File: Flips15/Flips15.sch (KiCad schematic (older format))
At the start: 6 parts

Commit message: Flips15 to only use 1 unit
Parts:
- removed CNX101: UFP2810, Own:Pin_Header_Angle_Shrouded_2x05_Pitch2.54mm_ConvNumbering, symbol Eigene~Bauteile:UFP2810
- added JP101, JP102, JP103, JP104, JP105, JP106, JP107, JP108, JP109, JP110, JP111, JP112, JP113, JP114, JP115, JP116, JP117, JP118, JP119, JP120, JP121, JP122, JP123, JP124, JP125, JP126, JP127, JP128: Jumper_NO_Small, Own:SolderJumper1.3mm, symbol Device:Jumper_NO_Small
- BRDIC1: renamed from BRDIC101; footprint Own:Pin_Header_Angle_Shrouded_2x17_Pitch2.54mm_ConvNumbering -> Own:Pin_Header_Straight_Shrouded_Locks_2x17_Pitch2.54mm_ConvNumbering
- BROSE20: renamed from BROSE103; footprint Own:Pin_Header_Straight_Shrouded_2x10_Pitch2.54mm_ConvNumbering -> Own:Pin_Header_Straight_Shrouded_Locks_2x10_Pitch2.54mm_ConvNumbering
- BROSE34: renamed from BROSE102; footprint Own:Pin_Header_Angle_Shrouded_2x17_Pitch2.54mm_ConvNumbering -> Own:Pin_Header_Straight_Shrouded_Locks_2x17_Pitch2.54mm_ConvNumbering
- BROSE60: renamed from BROSE101; footprint Own:Pin_Header_Straight_Shrouded_2x30_Pitch2.54mm_ConvNumbering -> Own:Pin_Header_Straight_Shrouded_Locks_2x30_Pitch2.54mm_ConvNumbering
- renumbered CNY101 to CN1
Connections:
- wire segments 160 -> 80
- no-connect marks 66 -> 58

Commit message: experimenting with solder jumpers at BRDIC1 connector
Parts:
- JP101, JP102, JP103, JP104, JP105, JP106, JP107, JP108, JP109, JP110, JP111, JP112, JP113, JP114, JP115, JP116, JP117, JP118, JP119, JP120, JP121, JP122, JP123, JP124, JP125, JP126, JP127, JP128: footprint Own:SolderJumper1.3mm -> Own:SolderJumper1.3mmNoSilk
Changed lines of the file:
@@
 F 0 "JP114" H 7900 3393 50  0000 C CNN
 F 1 "Jumper_NO_Small" H 7900 3394 50  0001 C CNN
-F 2 "Own:SolderJumper1.3mm" H 7900 3300 50  0001 C CNN
+F 2 "Own:SolderJumper1.3mmNoSilk" H 7900 3300 50  0001 C CNN
 F 3 "~" H 7900 3300 50  0001 C CNN
 	1    7900 3300
@@
 F 0 "JP113" H 7900 3293 50  0000 C CNN
 F 1 "Jumper_NO_Small" H 7900 3294 50  0001 C CNN
-F 2 "Own:SolderJumper1.3mm" H 7900 3200 50  0001 C CNN
+F 2 "Own:SolderJumper1.3mmNoSilk" H 7900 3200 50  0001 C CNN
 F 3 "~" H 7900 3200 50  0001 C CNN
 	1    7900 3200
@@
 F 0 "JP112" H 7900 3193 50  0000 C CNN
 F 1 "Jumper_NO_Small" H 7900 3194 50  0001 C CNN
-F 2 "Own:SolderJumper1.3mm" H 7900 3100 50  0001 C CNN
+F 2 "Own:SolderJumper1.3mmNoSilk" H 7900 3100 50  0001 C CNN
 F 3 "~" H 7900 3100 50  0001 C CNN
 	1    7900 3100
@@
 F 0 "JP111" H 7900 3093 50  0000 C CNN
 F 1 "Jumper_NO_Small" H 7900 3094 50  0001 C CNN
-F 2 "Own:SolderJumper1.3mm" H 7900 3000 50  0001 C CNN
+F 2 "Own:SolderJumper1.3mmNoSilk" H 7900 3000 50  0001 C CNN
 F 3 "~" H 7900 3000 50  0001 C CNN
 	1    7900 3000
@@
 F 0 "JP110" H 7900 2993 50  0000 C CNN
 F 1 "Jumper_NO_Small" H 7900 2994 50  0001 C CNN
-F 2 "Own:SolderJumper1.3mm" H 7900 2900 50  0001 C CNN
+F 2 "Own:SolderJumper1.3mmNoSilk" H 7900 2900 50  0001 C CNN
 F 3 "~" H 7900 2900 50  0001 C CNN
 	1    7900 2900
@@
 F 0 "JP109" H 7900 2893 50  0000 C CNN
 F 1 "Jumper_NO_Small" H 7900 2894 50  0001 C CNN
-F 2 "Own:SolderJumper1.3mm" H 7900 2800 50  0001 C CNN
+F 2 "Own:SolderJumper1.3mmNoSilk" H 7900 2800 50  0001 C CNN
 F 3 "~" H 7900 2800 50  0001 C CNN
 	1    7900 2800
@@
 F 0 "JP108" H 7900 2793 50  0000 C CNN
 F 1 "Jumper_NO_Small" H 7900 2794 50  0001 C CNN
-F 2 "Own:SolderJumper1.3mm" H 7900 2700 50  0001 C CNN
+F 2 "Own:SolderJumper1.3mmNoSilk" H 7900 2700 50  0001 C CNN
 F 3 "~" H 7900 2700 50  0001 C CNN
 	1    7900 2700
@@
 F 0 "JP107" H 7900 2293 50  0000 C CNN
 F 1 "Jumper_NO_Small" H 7900 2294 50  0001 C CNN
-F 2 "Own:SolderJumper1.3mm" H 7900 2200 50  0001 C CNN
+F 2 "Own:SolderJumper1.3mmNoSilk" H 7900 2200 50  0001 C CNN
 F 3 "~" H 7900 2200 50  0001 C CNN
 	1    7900 2200
@@
 F 0 "JP106" H 7900 2193 50  0000 C CNN
 F 1 "Jumper_NO_Small" H 7900 2194 50  0001 C CNN
-F 2 "Own:SolderJumper1.3mm" H 7900 2100 50  0001 C CNN
+F 2 "Own:SolderJumper1.3mmNoSilk" H 7900 2100 50  0001 C CNN
 F 3 "~" H 7900 2100 50  0001 C CNN
 	1    7900 2100
@@
 F 0 "JP105" H 7900 2093 50  0000 C CNN
 F 1 "Jumper_NO_Small" H 7900 2094 50  0001 C CNN
-F 2 "Own:SolderJumper1.3mm" H 7900 2000 50  0001 C CNN
+F 2 "Own:SolderJumper1.3mmNoSilk" H 7900 2000 50  0001 C CNN
 F 3 "~" H 7900 2000 50  0001 C CNN
 	1    7900 2000
@@
 F 0 "JP104" H 7900 1993 50  0000 C CNN
 F 1 "Jumper_NO_Small" H 7900 1994 50  0001 C CNN
-F 2 "Own:SolderJumper1.3mm" H 7900 1900 50  0001 C CNN
+F 2 "Own:SolderJumper1.3mmNoSilk" H 7900 1900 50  0001 C CNN
 F 3 "~" H 7900 1900 50  0001 C CNN
 	1    7900 1900
@@
 F 0 "JP103" H 7900 1893 50  0000 C CNN
 F 1 "Jumper_NO_Small" H 7900 1894 50  0001 C CNN
-F 2 "Own:SolderJumper1.3mm" H 7900 1800 50  0001 C CNN
+F 2 "Own:SolderJumper1.3mmNoSilk" H 7900 1800 50  0001 C CNN
 F 3 "~" H 7900 1800 50  0001 C CNN
 	1    7900 1800
@@
 F 0 "JP102" H 7900 1793 50  0000 C CNN
 F 1 "Jumper_NO_Small" H 7900 1794 50  0001 C CNN
-F 2 "Own:SolderJumper1.3mm" H 7900 1700 50  0001 C CNN
+F 2 "Own:SolderJumper1.3mmNoSilk" H 7900 1700 50  0001 C CNN
 F 3 "~" H 7900 1700 50  0001 C CNN
 	1    7900 1700
@@
 F 0 "JP101" H 7900 1693 50  0000 C CNN
 F 1 "Jumper_NO_Small" H 7900 1694 50  0001 C CNN
-F 2 "Own:SolderJumper1.3mm" H 7900 1600 50  0001 C CNN
+F 2 "Own:SolderJumper1.3mmNoSilk" H 7900 1600 50  0001 C CNN
 F 3 "~" H 7900 1600 50  0001 C CNN
 	1    7900 1600
@@
 F 0 "JP121" H 7900 4493 50  0000 C CNN
 F 1 "Jumper_NO_Small" H 7900 4494 50  0001 C CNN
-F 2 "Own:SolderJumper1.3mm" H 7900 4400 50  0001 C CNN
+F 2 "Own:SolderJumper1.3mmNoSilk" H 7900 4400 50  0001 C CNN
 F 3 "~" H 7900 4400 50  0001 C CNN
 	1    7900 4400
@@
 F 0 "JP120" H 7900 4393 50  0000 C CNN
 F 1 "Jumper_NO_Small" H 7900 4394 50  0001 C CNN
-F 2 "Own:SolderJumper1.3mm" H 7900 4300 50  0001 C CNN
+F 2 "Own:SolderJumper1.3mmNoSilk" H 7900 4300 50  0001 C CNN
 F 3 "~" H 7900 4300 50  0001 C CNN
 	1    7900 4300
@@
 F 0 "JP119" H 7900 4293 50  0000 C CNN
 F 1 "Jumper_NO_Small" H 7900 4294 50  0001 C CNN
-F 2 "Own:SolderJumper1.3mm" H 7900 4200 50  0001 C CNN
+F 2 "Own:SolderJumper1.3mmNoSilk" H 7900 4200 50  0001 C CNN
 F 3 "~" H 7900 4200 50  0001 C CNN
 	1    7900 4200
@@
 F 0 "JP118" H 7900 4193 50  0000 C CNN
 F 1 "Jumper_NO_Small" H 7900 4194 50  0001 C CNN
-F 2 "Own:SolderJumper1.3mm" H 7900 4100 50  0001 C CNN
+F 2 "Own:SolderJumper1.3mmNoSilk" H 7900 4100 50  0001 C CNN
 F 3 "~" H 7900 4100 50  0001 C CNN
 	1    7900 4100
@@
 F 0 "JP117" H 7900 4093 50  0000 C CNN
 F 1 "Jumper_NO_Small" H 7900 4094 50  0001 C CNN
-F 2 "Own:SolderJumper1.3mm" H 7900 4000 50  0001 C CNN
+F 2 "Own:SolderJumper1.3mmNoSilk" H 7900 4000 50  0001 C CNN
 F 3 "~" H 7900 4000 50  0001 C CNN
 	1    7900 4000
@@
 F 0 "JP116" H 7900 3993 50  0000 C CNN
 F 1 "Jumper_NO_Small" H 7900 3994 50  0001 C CNN
-F 2 "Own:SolderJumper1.3mm" H 7900 3900 50  0001 C CNN
+F 2 "Own:SolderJumper1.3mmNoSilk" H 7900 3900 50  0001 C CNN
 F 3 "~" H 7900 3900 50  0001 C CNN
 	1    7900 3900
@@
 F 0 "JP115" H 7900 3893 50  0000 C CNN
 F 1 "Jumper_NO_Small" H 7900 3894 50  0001 C CNN
-F 2 "Own:SolderJumper1.3mm" H 7900 3800 50  0001 C CNN
+F 2 "Own:SolderJumper1.3mmNoSilk" H 7900 3800 50  0001 C CNN
 F 3 "~" H 7900 3800 50  0001 C CNN
 	1    7900 3800
@@
 F 0 "JP128" H 7900 5593 50  0000 C CNN
 F 1 "Jumper_NO_Small" H 7900 5594 50  0001 C CNN
-F 2 "Own:SolderJumper1.3mm" H 7900 5500 50  0001 C CNN
+F 2 "Own:SolderJumper1.3mmNoSilk" H 7900 5500 50  0001 C CNN
 F 3 "~" H 7900 5500 50  0001 C CNN
 	1    7900 5500
@@
 F 0 "JP127" H 7900 5493 50  0000 C CNN
 F 1 "Jumper_NO_Small" H 7900 5494 50  0001 C CNN
-F 2 "Own:SolderJumper1.3mm" H 7900 5400 50  0001 C CNN
+F 2 "Own:SolderJumper1.3mmNoSilk" H 7900 5400 50  0001 C CNN
 F 3 "~" H 7900 5400 50  0001 C CNN
 	1    7900 5400
@@
 F 0 "JP126" H 7900 5393 50  0000 C CNN
 F 1 "Jumper_NO_Small" H 7900 5394 50  0001 C CNN
-F 2 "Own:SolderJumper1.3mm" H 7900 5300 50  0001 C CNN
+F 2 "Own:SolderJumper1.3mmNoSilk" H 7900 5300 50  0001 C CNN
 F 3 "~" H 7900 5300 50  0001 C CNN
 	1    7900 5300
@@
 F 0 "JP125" H 7900 5293 50  0000 C CNN
 F 1 "Jumper_NO_Small" H 7900 5294 50  0001 C CNN
-F 2 "Own:SolderJumper1.3mm" H 7900 5200 50  0001 C CNN
+F 2 "Own:SolderJumper1.3mmNoSilk" H 7900 5200 50  0001 C CNN
 F 3 "~" H 7900 5200 50  0001 C CNN
 	1    7900 5200
@@
 F 0 "JP124" H 7900 5193 50  0000 C CNN
 F 1 "Jumper_NO_Small" H 7900 5194 50  0001 C CNN
-F 2 "Own:SolderJumper1.3mm" H 7900 5100 50  0001 C CNN
+F 2 "Own:SolderJumper1.3mmNoSilk" H 7900 5100 50  0001 C CNN
 F 3 "~" H 7900 5100 50  0001 C CNN
 	1    7900 5100
@@
 F 0 "JP123" H 7900 5093 50  0000 C CNN
 F 1 "Jumper_NO_Small" H 7900 5094 50  0001 C CNN
-F 2 "Own:SolderJumper1.3mm" H 7900 5000 50  0001 C CNN
+F 2 "Own:SolderJumper1.3mmNoSilk" H 7900 5000 50  0001 C CNN
 F 3 "~" H 7900 5000 50  0001 C CNN
 	1    7900 5000
@@
 F 0 "JP122" H 7900 4993 50  0000 C CNN
 F 1 "Jumper_NO_Small" H 7900 4994 50  0001 C CNN
-F 2 "Own:SolderJumper1.3mm" H 7900 4900 50  0001 C CNN
+F 2 "Own:SolderJumper1.3mmNoSilk" H 7900 4900 50  0001 C CNN
 F 3 "~" H 7900 4900 50  0001 C CNN
 	1    7900 4900

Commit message: more tracing with overlapping connectors
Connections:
- net labels added: T5, T7, T8
- no-connect marks 58 -> 47
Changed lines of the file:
@@
 X28
 NoConn ~ 10200 2100
-NoConn ~ 10200 3100
 NoConn ~ 10700 2200
 NoConn ~ 10700 1600
@@
 	1    0    0    -1
 $EndComp
-NoConn ~ 10700 3200
-NoConn ~ 10200 3200
 $Comp
 L Connector_Generic:Conn_02x17_Odd_Even BROSE34
@@
 Text Label 1800 5700 0    50   ~ 0
 ~RY7
-NoConn ~ 1800 4200
-NoConn ~ 1300 4200
-NoConn ~ 1300 4300
-NoConn ~ 1300 4400
-NoConn ~ 1300 4500
 NoConn ~ 1300 4600
 NoConn ~ 1300 4700
@@
 NoConn ~ 1800 4700
 NoConn ~ 1800 4600
-NoConn ~ 1800 4500
-NoConn ~ 1800 4400
-NoConn ~ 1800 4300
 $Comp
 L Connector_Generic:Conn_02x10_Odd_Even BROSE20
@@
 	1    0    0    -1
 $EndComp
+Text Label 10700 3200 0    50   ~ 0
+T8
+Text Label 10200 3100 2    50   ~ 0
+T5
+Text Label 10200 3200 2    50   ~ 0
+T7
+Text Label 1300 4200 2    50   ~ 0
+X23
+Text Label 1300 4300 2    50   ~ 0
+X22
+Text Label 1300 4400 2    50   ~ 0
+T5
+Text Label 1300 4500 2    50   ~ 0
+T7
+Text Label 1800 4200 0    50   ~ 0
+X3
+Text Label 1800 4300 0    50   ~ 0
+X2
+Text Label 1800 4400 0    50   ~ 0
+X1
+Text Label 1800 4500 0    50   ~ 0
+T8
 $EndSCHEMATC

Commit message: Adding more solder jumpers to overlapping pins of BRDIC1 and BROSE34
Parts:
- added JP129, JP130, JP131, JP132, JP133: Jumper_NO_Small, Own:SolderJumper1.3mmNoSilk, symbol Device:Jumper_NO_Small
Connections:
- net labels added: T1, T2, T3, T4, T6
- wire segments 80 -> 88
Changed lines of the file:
@@
 Text Label 8150 4400 0    50   ~ 0
 ~RY21
-Text Label 8150 5000 0    50   ~ 0
+Text Label 9200 5000 2    50   ~ 0
 ~RY23
 Text Label 8150 5200 0    50   ~ 0
@@
 Text Label 7550 5500 2    50   ~ 0
 SY28
-Text Label 8150 4900 0    50   ~ 0
+Text Label 9200 4900 2    50   ~ 0
 ~RY22
 Text Label 8150 5100 0    50   ~ 0
@@
 Text Label 7550 3300 2    50   ~ 0
 SY14
-Text Label 8300 1700 2    50   ~ 0
+Text Label 9150 1700 2    50   ~ 0
 ~RY2
 Text Label 8300 1900 2    50   ~ 0
@@
 Text Label 8350 3300 2    50   ~ 0
 ~RY14
-Text Label 8300 1600 2    50   ~ 0
+Text Label 9150 1600 2    50   ~ 0
 ~RY1
-Text Label 8300 1800 2    50   ~ 0
+Text Label 9150 1800 2    50   ~ 0
 ~RY3
 Text Label 8300 2000 2    50   ~ 0
@@
 	1    0    0    -1
 $EndComp
-Text Label 10700 3200 0    50   ~ 0
+Text Label 10950 3200 0    50   ~ 0
 T8
-Text Label 10200 3100 2    50   ~ 0
+Text Label 9950 3100 2    50   ~ 0
 T5
-Text Label 10200 3200 2    50   ~ 0
+Text Label 9950 3200 2    50   ~ 0
 T7
-Text Label 1300 4200 2    50   ~ 0
-X23
-Text Label 1300 4300 2    50   ~ 0
-X22
 Text Label 1300 4400 2    50   ~ 0
 T5
 Text Label 1300 4500 2    50   ~ 0
 T7
-Text Label 1800 4200 0    50   ~ 0
-X3
-Text Label 1800 4300 0    50   ~ 0
-X2
-Text Label 1800 4400 0    50   ~ 0
-X1
 Text Label 1800 4500 0    50   ~ 0
 T8
+$Comp
+L Device:Jumper_NO_Small JP130
+U 1 1 5C5630B2
+P 9250 1800
+F 0 "JP130" H 9250 1893 50  0000 C CNN
+F 1 "Jumper_NO_Small" H 9250 1894 50  0001 C CNN
+F 2 "Own:SolderJumper1.3mmNoSilk" H 9250 1800 50  0001 C CNN
+F 3 "~" H 9250 1800 50  0001 C CNN
+	1    9250 1800
+	1    0    0    -1
+$EndComp
+$Comp
+L Device:Jumper_NO_Small JP132
+U 1 1 5C56350E
+P 9250 1700
+F 0 "JP132" H 9250 1793 50  0000 C CNN
+F 1 "Jumper_NO_Small" H 9250 1794 50  0001 C CNN
+F 2 "Own:SolderJumper1.3mmNoSilk" H 9250 1700 50  0001 C CNN
+F 3 "~" H 9250 1700 50  0001 C CNN
+	1    9250 1700
+	1    0    0    -1
+$EndComp
+$Comp
+L Device:Jumper_NO_Small JP133
+U 1 1 5C563564
+P 9250 1600
+F 0 "JP133" H 9250 1693 50  0000 C CNN
+F 1 "Jumper_NO_Small" H 9250 1694 50  0001 C CNN
+F 2 "Own:SolderJumper1.3mmNoSilk" H 9250 1600 50  0001 C CNN
+F 3 "~" H 9250 1600 50  0001 C CNN
+	1    9250 1600
+	1    0    0    -1
+$EndComp
+$Comp
+L Device:Jumper_NO_Small JP129
+U 1 1 5C5635BC
+P 9300 5000
+F 0 "JP129" H 9300 5093 50  0000 C CNN
+F 1 "Jumper_NO_Small" H 9300 5094 50  0001 C CNN
+F 2 "Own:SolderJumper1.3mmNoSilk" H 9300 5000 50  0001 C CNN
+F 3 "~" H 9300 5000 50  0001 C CNN
+	1    9300 5000
+	1    0    0    -1
+$EndComp
+$Comp
+L Device:Jumper_NO_Small JP131
+U 1 1 5C56362C
+P 9300 4900
+F 0 "JP131" H 9300 4993 50  0000 C CNN
+F 1 "Jumper_NO_Small" H 9300 4994 50  0001 C CNN
+F 2 "Own:SolderJumper1.3mmNoSilk" H 9300 4900 50  0001 C CNN
+F 3 "~" H 9300 4900 50  0001 C CNN
+	1    9300 4900
+	1    0    0    -1
+$EndComp
+Text Label 1300 4300 2    50   ~ 0
+T3
+Text Label 1300 4200 2    50   ~ 0
+T1
+Text Label 1800 4200 0    50   ~ 0
+T2
+Text Label 1800 4300 0    50   ~ 0
+T4
+Text Label 1800 4400 0    50   ~ 0
+T6
+Text Label 9950 2900 2    50   ~ 0
+T1
+Text Label 9950 3000 2    50   ~ 0
+T3
+Text Label 10950 2900 0    50   ~ 0
+T2
+Text Label 10950 3000 0    50   ~ 0
+T4
+Text Label 10950 3100 0    50   ~ 0
+T6
+Wire Wire Line
+	10700 2900 10950 2900
+Wire Wire Line
+	10700 3000 10950 3000
+Wire Wire Line
+	10700 3100 10950 3100
+Wire Wire Line
+	9950 2900 10200 2900
+Wire Wire Line
+	9950 3000 10200 3000
+Wire Wire Line
+	10200 3100 9950 3100
+Wire Wire Line
+	9950 3200 10200 3200
+Wire Wire Line
+	10700 3200 10950 3200
+Text Label 9400 5000 0    50   ~ 0
+X23
+Text Label 9400 4900 0    50   ~ 0
+X22
+Text Label 9350 1800 0    50   ~ 0
+X3
+Text Label 9350 1700 0    50   ~ 0
+X2
+Text Label 9350 1600 0    50   ~ 0
+X1
 $EndSCHEMATC

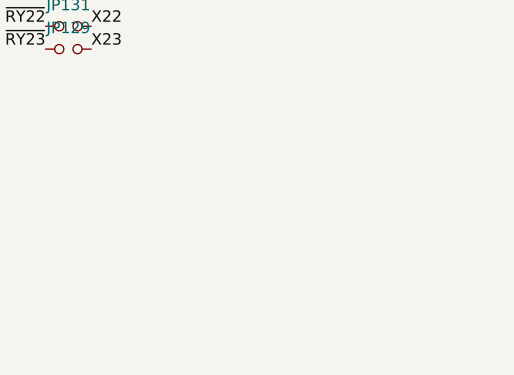
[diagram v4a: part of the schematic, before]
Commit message: adding mounting holes, more traces
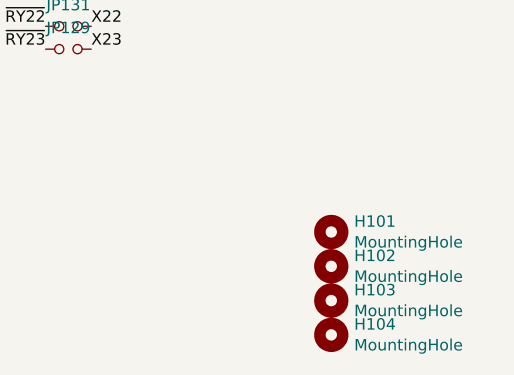
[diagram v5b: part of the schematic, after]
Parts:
- added H101, H102, H103, H104: MountingHole, Mounting_Holes:MountingHole_3.2mm_M3_ISO14580_Pad, symbol Mechanical:MountingHole
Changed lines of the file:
@@
 Text Label 9350 1600 0    50   ~ 0
 X1
+$Comp
+L Mechanical:MountingHole H101
+U 1 1 5C564F22
+P 10450 5800
+F 0 "H101" H 10550 5846 50  0000 L CNN
+F 1 "MountingHole" H 10550 5755 50  0000 L CNN
+F 2 "Mounting_Holes:MountingHole_3.2mm_M3_ISO14580_Pad" H 10450 5800 50  0001 C CNN
+F 3 "~" H 10450 5800 50  0001 C CNN
+	1    10450 5800
+	1    0    0    -1
+$EndComp
+$Comp
+L Mechanical:MountingHole H102
+U 1 1 5C565189
+P 10450 5950
+F 0 "H102" H 10550 5996 50  0000 L CNN
+F 1 "MountingHole" H 10550 5905 50  0000 L CNN
+F 2 "Mounting_Holes:MountingHole_3.2mm_M3_ISO14580_Pad" H 10450 5950 50  0001 C CNN
+F 3 "~" H 10450 5950 50  0001 C CNN
+	1    10450 5950
+	1    0    0    -1
+$EndComp
+$Comp
+L Mechanical:MountingHole H103
+U 1 1 5C5651EF
+P 10450 6100
+F 0 "H103" H 10550 6146 50  0000 L CNN
+F 1 "MountingHole" H 10550 6055 50  0000 L CNN
+F 2 "Mounting_Holes:MountingHole_3.2mm_M3_ISO14580_Pad" H 10450 6100 50  0001 C CNN
+F 3 "~" H 10450 6100 50  0001 C CNN
+	1    10450 6100
+	1    0    0    -1
+$EndComp
+$Comp
+L Mechanical:MountingHole H104
+U 1 1 5C565255
+P 10450 6250
+F 0 "H104" H 10550 6296 50  0000 L CNN
+F 1 "MountingHole" H 10550 6205 50  0000 L CNN
+F 2 "Mounting_Holes:MountingHole_3.2mm_M3_ISO14580_Pad" H 10450 6250 50  0001 C CNN
+F 3 "~" H 10450 6250 50  0001 C CNN
+	1    10450 6250
+	1    0    0    -1
+$EndComp
 $EndSCHEMATC

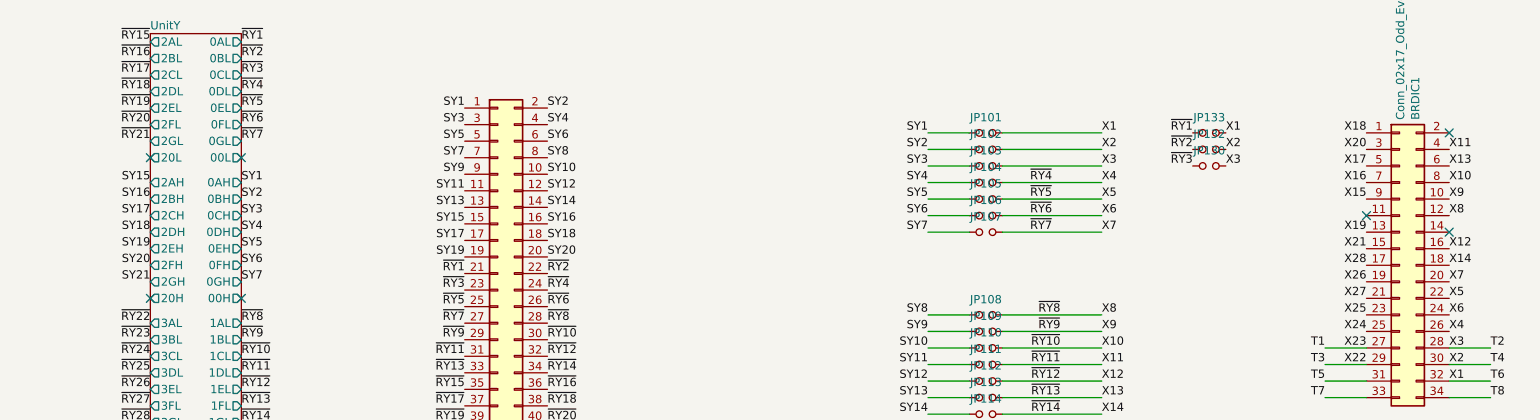
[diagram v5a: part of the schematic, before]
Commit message: adding support for optional COM pin at BRDIC1
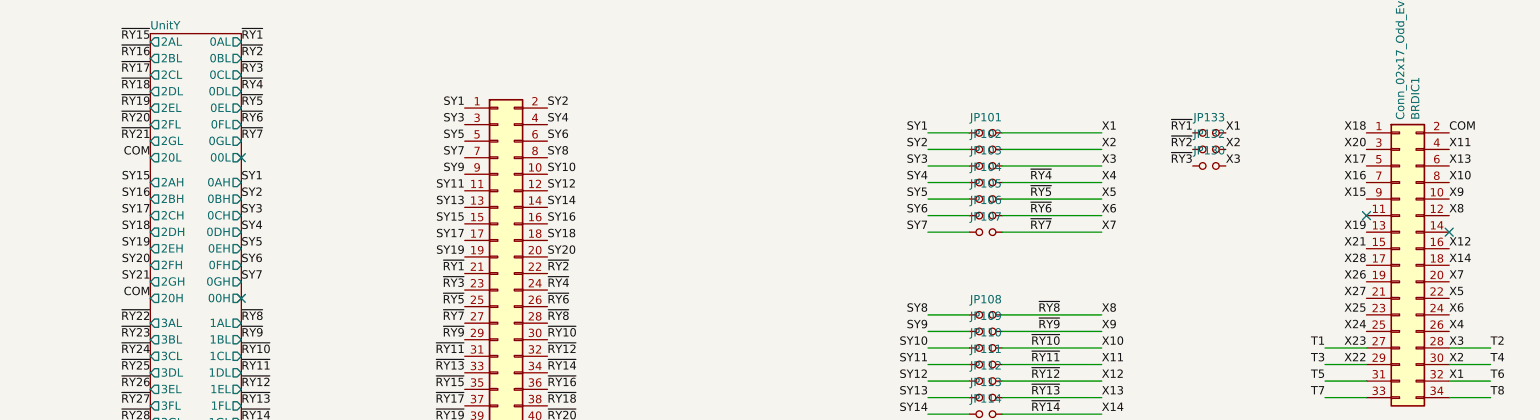
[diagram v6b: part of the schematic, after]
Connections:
- net labels added: COM
- no-connect marks 47 -> 44
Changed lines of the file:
@@
 NoConn ~ 10200 2100
 NoConn ~ 10700 2200
-NoConn ~ 10700 1600
 $Comp
 L Connector_Generic:Conn_02x17_Odd_Even BRDIC1
@@
 NoConn ~ 3400 3450
 NoConn ~ 3400 4300
-NoConn ~ 2850 1750
-NoConn ~ 2850 2600
 NoConn ~ 2850 3450
 NoConn ~ 2850 4300
@@
 	1    0    0    -1
 $EndComp
+Text Label 10700 1600 0    50   ~ 0
+COM
+Text Label 2850 1750 2    50   ~ 0
+COM
+Text Label 2850 2600 2    50   ~ 0
+COM
 $EndSCHEMATC
